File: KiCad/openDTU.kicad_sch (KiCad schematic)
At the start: 9 parts, among them U1 ESP32NodeMCU, U2 NRF24L01+PA+LNA_Breakout

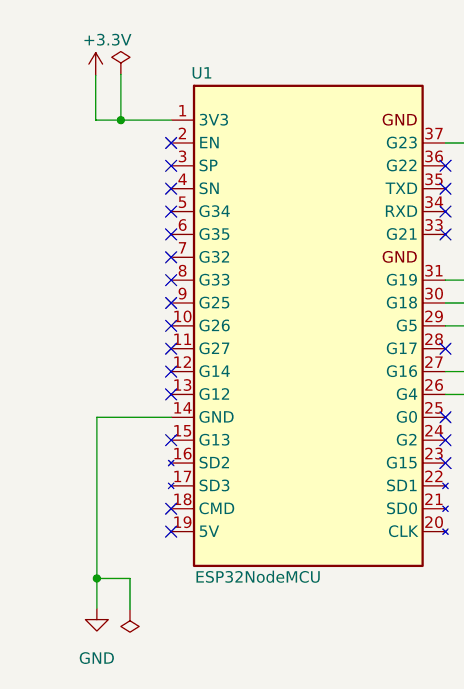
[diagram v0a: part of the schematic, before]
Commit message: Added mounting holes and some other improvments
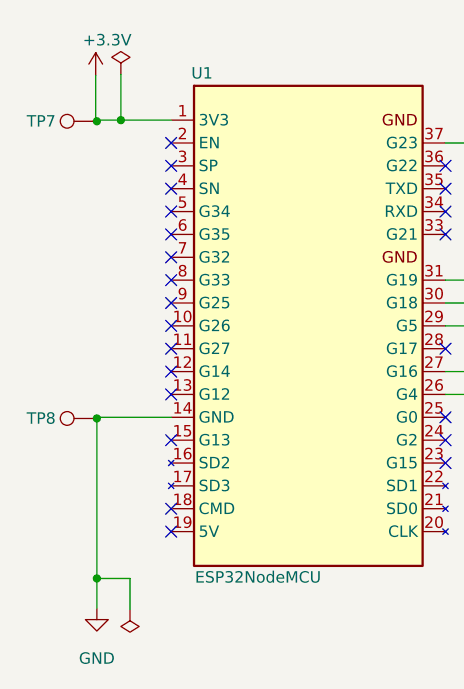
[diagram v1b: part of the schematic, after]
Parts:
- added TP7, TP8: TestPoint, TestPoint:TestPoint_THTPad_D1.5mm_Drill0.7mm, symbol Connector:TestPoint
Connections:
- net GND: now also TP8.1
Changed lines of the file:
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@@
   (junction (at 78.74 128.27) (diameter 0) (color 0 0 0 0)
+  )
+  (junction (at 78.74 110.49) (diameter 0) (color 0 0 0 0)
+  )
+  (junction (at 78.74 77.47) (diameter 0) (color 0 0 0 0)
   )
   (no_connect (at 86.995 123.063))
@@
     (stroke (width 0) (type default) (color 0 0 0 0))
   )
-  (wire (pts (xy 78.74 128.27) (xy 78.74 110.363))
+  (wire (pts (xy 78.74 128.27) (xy 78.74 110.49))
     (stroke (width 0) (type default) (color 0 0 0 0))
   )
@@
   )
   (wire (pts (xy 81.407 77.343) (xy 86.995 77.343))
+    (stroke (width 0) (type default) (color 0 0 0 0))
+  )
+  (wire (pts (xy 78.74 110.49) (xy 78.74 110.363))
     (stroke (width 0) (type default) (color 0 0 0 0))
   )
@@
     (pin "8")
   )
+  (symbol (lib_id "Connector:TestPoint") (at 78.74 110.49 90) (unit 1)
+    (in_bom yes) (on_board yes)
+    (property "Reference" "TP8" (id 0) (at 74.168 110.49 90)
+      (effects (font (size 1.27 1.27)) (justify left))
+    )
+    (property "Value" "TestPoint" (id 1) (at 73.533 109.2201 90)
+      (effects (font (size 1.27 1.27)) (justify left) hide)
+    )
+    (property "Footprint" "TestPoint:TestPoint_THTPad_D1.5mm_Drill0.7mm" (id 2) (at 78.74 105.41 0)
+      (effects (font (size 1.27 1.27)) hide)
+    )
+    (property "Datasheet" "~" (id 3) (at 78.74 105.41 0)
+      (effects (font (size 1.27 1.27)) hide)
+    )
+    (pin "1")
+  )
   (symbol (lib_id "Connector:TestPoint") (at 124.333 79.883 270) (unit 1)
     (in_bom yes) (on_board yes)
@@
     (pin "1")
   )
+  (symbol (lib_id "Connector:TestPoint") (at 78.74 77.47 90) (unit 1)
+    (in_bom yes) (on_board yes)
+    (property "Reference" "TP7" (id 0) (at 74.168 77.47 90)
+      (effects (font (size 1.27 1.27)) (justify left))
+    )
+    (property "Value" "TestPoint" (id 1) (at 73.533 76.2001 90)
+      (effects (font (size 1.27 1.27)) (justify left) hide)
+    )
+    (property "Footprint" "TestPoint:TestPoint_THTPad_D1.5mm_Drill0.7mm" (id 2) (at 78.74 72.39 0)
+      (effects (font (size 1.27 1.27)) hide)
+    )
+    (property "Datasheet" "~" (id 3) (at 78.74 72.39 0)
+      (effects (font (size 1.27 1.27)) hide)
+    )
+    (pin "1")
+  )
   (symbol (lib_id "power:GND") (at 205.867 83.439 0) (unit 1)
     (in_bom yes) (on_board yes)
@@
       (reference "TP6") (unit 1) (value "TestPoint") (footprint "TestPoint:TestPoint_THTPad_D1.5mm_Drill0.7mm")
     )
+    (path "/f22f12ac-7be9-4229-8bbf-b72fc56965c9"
+      (reference "TP7") (unit 1) (value "TestPoint") (footprint "TestPoint:TestPoint_THTPad_D1.5mm_Drill0.7mm")
+    )
+    (path "/7d49c6c1-d16a-4f91-b21c-7492e3335374"
+      (reference "TP8") (unit 1) (value "TestPoint") (footprint "TestPoint:TestPoint_THTPad_D1.5mm_Drill0.7mm")
+    )
     (path "/0626e94d-7e2b-4dab-a267-2ede4e5d9e77"
